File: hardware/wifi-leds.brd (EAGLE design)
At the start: 108 x 81 mm, 30 parts, among them IC2 LDL112D33R, Q2 FQP30N06L, U1 ESP-WROOM-32

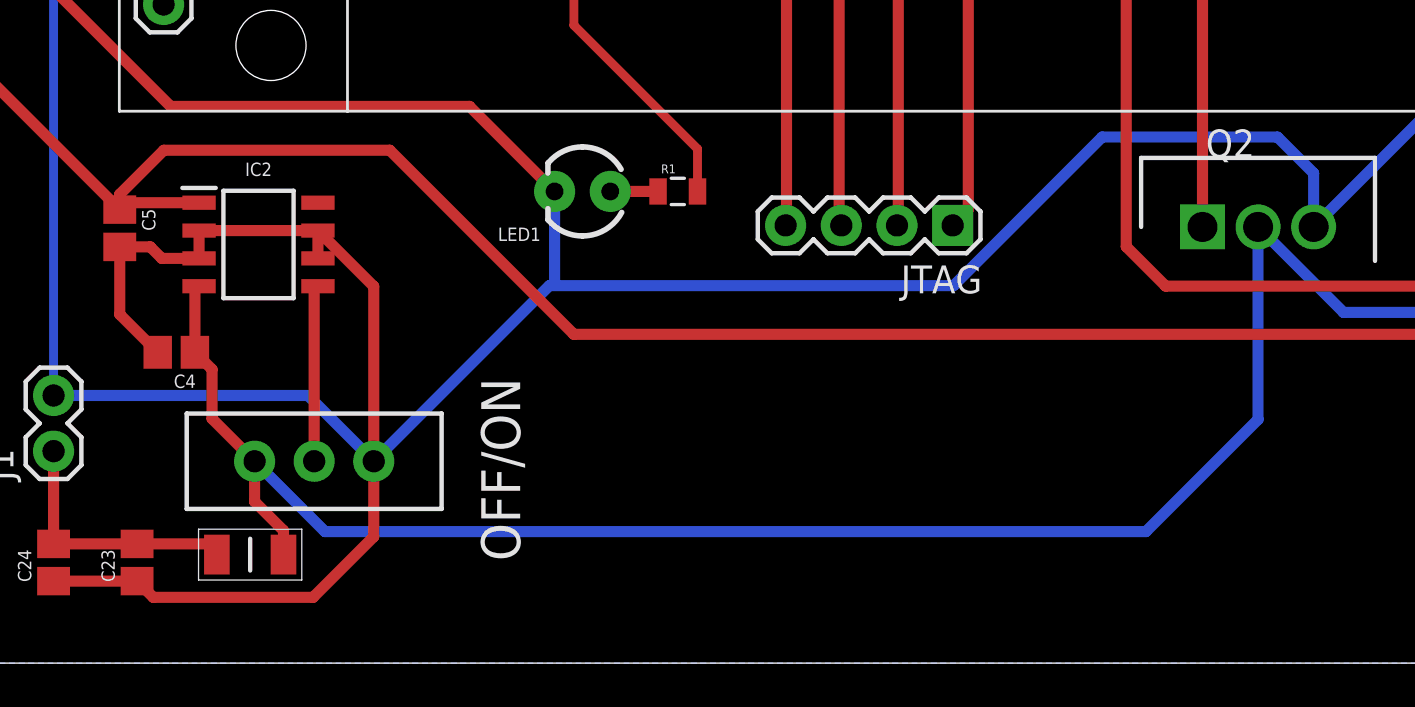
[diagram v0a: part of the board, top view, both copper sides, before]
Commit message: updated ignore, minor trace moves
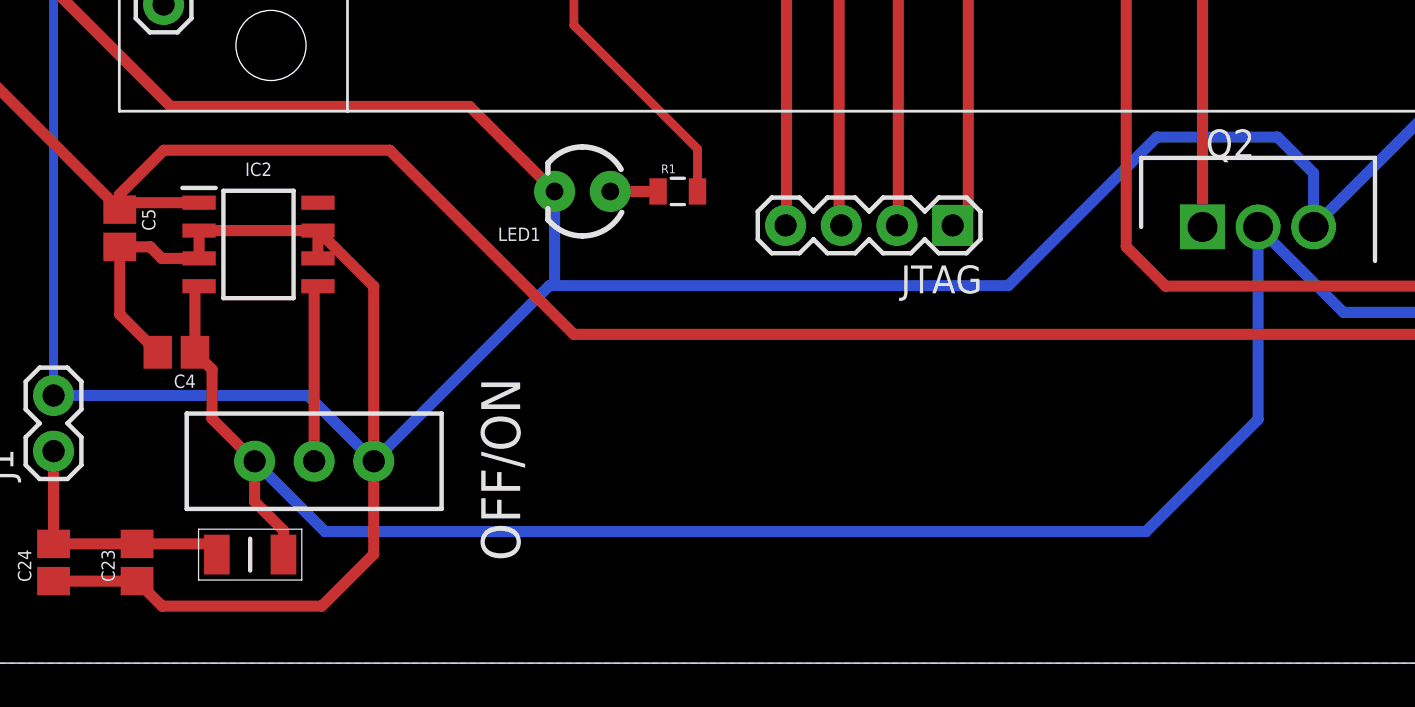
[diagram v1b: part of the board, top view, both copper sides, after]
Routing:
- net GND: track 445.2 -> 446.0 mm
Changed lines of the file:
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@@
 <wire x1="21.7678" y1="9.21" x2="21.7678" y2="17.1892" width="0.508" layer="1"/>
 <wire x1="21.7678" y1="17.1892" x2="19.222" y2="19.735" width="0.508" layer="1"/>
-<wire x1="10.97" y1="3.74" x2="11.71" y2="3" width="0.508" layer="1"/>
-<wire x1="11.71" y1="3" x2="19" y2="3" width="0.508" layer="1"/>
-<wire x1="19" y1="3" x2="21.767796875" y2="5.767796875" width="0.508" layer="1"/>
-<wire x1="21.767796875" y1="5.767796875" x2="21.7678" y2="9.21" width="0.508" layer="1"/>
+<wire x1="10.97" y1="3.74" x2="12.11" y2="2.6" width="0.508" layer="1"/>
+<wire x1="12.11" y1="2.6" x2="19.4" y2="2.6" width="0.508" layer="1"/>
+<wire x1="19.4" y1="2.6" x2="21.767796875" y2="4.967796875" width="0.508" layer="1"/>
+<wire x1="21.767796875" y1="4.967796875" x2="21.7678" y2="9.21" width="0.508" layer="1"/>
 <wire x1="7.16" y1="3.74" x2="10.97" y2="3.74" width="0.508" layer="1"/>
 <wire x1="21.7678" y1="9.21" x2="29.7789" y2="17.2211" width="0.508" layer="16"/>
 <wire x1="29.7789" y1="17.2211" x2="30.02" y2="17.4622" width="0.3048" layer="16"/>
 <wire x1="30.02" y1="17.4622" x2="30.02" y2="21.52" width="0.508" layer="16"/>
-<wire x1="29.7789" y1="17.2211" x2="48.2211" y2="17.2211" width="0.508" layer="16"/>
-<wire x1="55" y1="24" x2="63" y2="24" width="0.508" layer="16"/>
+<wire x1="29.7789" y1="17.2211" x2="50.7211" y2="17.2211" width="0.508" layer="16"/>
+<wire x1="57.5" y1="24" x2="63" y2="24" width="0.508" layer="16"/>
 <wire x1="63" y1="24" x2="64.65" y2="22.35" width="0.508" layer="16"/>
 <wire x1="64.65" y1="22.35" x2="64.65" y2="19.9" width="0.508" layer="16"/>
-<wire x1="48.2211" y1="17.2211" x2="55" y2="24" width="0.508" layer="16"/>
+<wire x1="50.7211" y1="17.2211" x2="57.5" y2="24" width="0.508" layer="16"/>
 <wire x1="64.65" y1="19.9" x2="80.65" y2="35.9" width="0.508" layer="16"/>
 <wire x1="80.65" y1="35.9" x2="88.5" y2="35.9" width="0.508" layer="16"/>

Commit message: added logo
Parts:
- added U$5: CMD_C0DE_LOGOCMD_CODE_LOGO_TOP_COPPER, logos:CMD_C0DE_LOGO_TOP_COPPER
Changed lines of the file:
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@@
 <attribute name="VALUE" x="61.31" y="16.28" size="1.27" layer="27" align="center"/>
 </element>
+<element name="U$5" library="logos" package="CMD_C0DE_LOGO_TOP_COPPER" value="CMD_C0DE_LOGOCMD_CODE_LOGO_TOP_COPPER" x="96" y="10" smashed="yes"/>
 </elements>
 <signals>

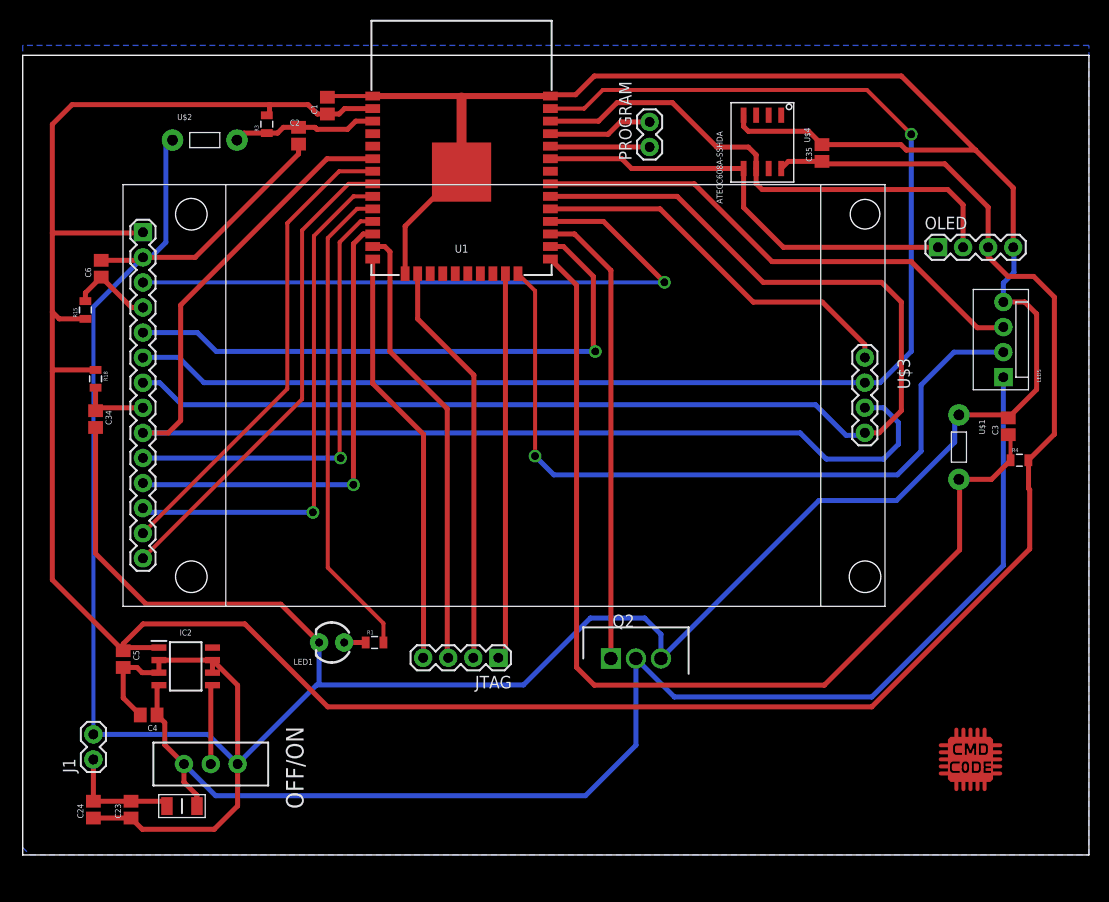
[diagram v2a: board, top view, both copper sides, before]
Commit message: shrunk foot print to fit on to a smaller fr4 board I have
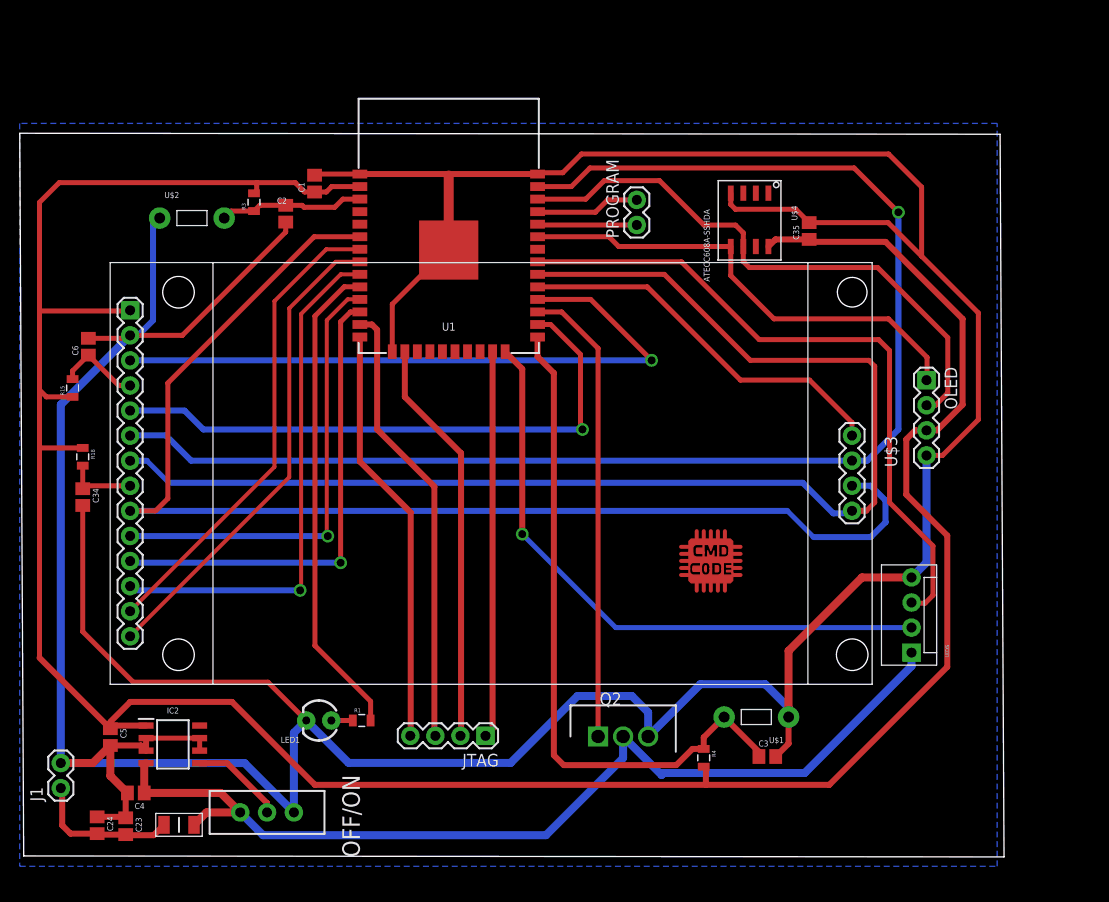
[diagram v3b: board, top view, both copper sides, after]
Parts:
- moved R4 43.9 mm to (69.0, 9.84), turned to 270 degrees
- moved C3 41.4 mm to (75.4, 9.97), turned to 0 degrees
- moved U$1 34.2 mm to (74.3, 14.0), turned to 180 degrees
- moved U$5 33.1 mm to (69.7, 30.1)
- moved LEDS 29.4 mm to (90.0, 20.5)
- moved OLED 13.5 mm to (91.5, 48.1), turned to 270 degrees
- moved C6 8.01 mm to (6.65, 51.5)
- moved R15 8.01 mm to (5.05, 47.3)
- moved U$3 8.01 mm to (8.86, 60.0)
- moved U$4 8.01 mm to (75.5, 67.0)
- moved IC2 8.01 mm to (15.2, 11.2)
- moved C5 8.01 mm to (8.88, 11.9)
- moved LED1 8.01 mm to (30.0, 13.6)
- moved R1 8.01 mm to (34.3, 13.6)
- moved U1 8.01 mm to (43.1, 61.3)
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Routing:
- net ESPIO0: track 103.6 -> 68.9 mm
- net VBAT: track 135.4 -> 100.8 mm
- net GND: track 446.0 -> 428.8 mm
- net LED_SCK: track 51.9 -> 68.7 mm
- net LED_MOSI: track 76.5 -> 62.5 mm
- net VCC: track 279.2 -> 273.0 mm
- net SCL: track 52.9 -> 58.9 mm
- net SDA: track 45.3 -> 48.6 mm
- net N$10: track 11.9 -> 15.0 mm
- net N$2: track 8.06 -> 9.44 mm
- net DISPLAY_SD_SCK: track 131.0 -> 129.9 mm
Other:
- board size 108 x 81 mm -> 99.7 x 73.3 mm
